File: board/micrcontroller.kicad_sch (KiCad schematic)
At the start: 20 parts, among them J2 USB_C_Receptacle_USB2.0_14P, SW1 SW_Push, U2 ESP32-S3-WROOM-1, U3 TXB0106PW

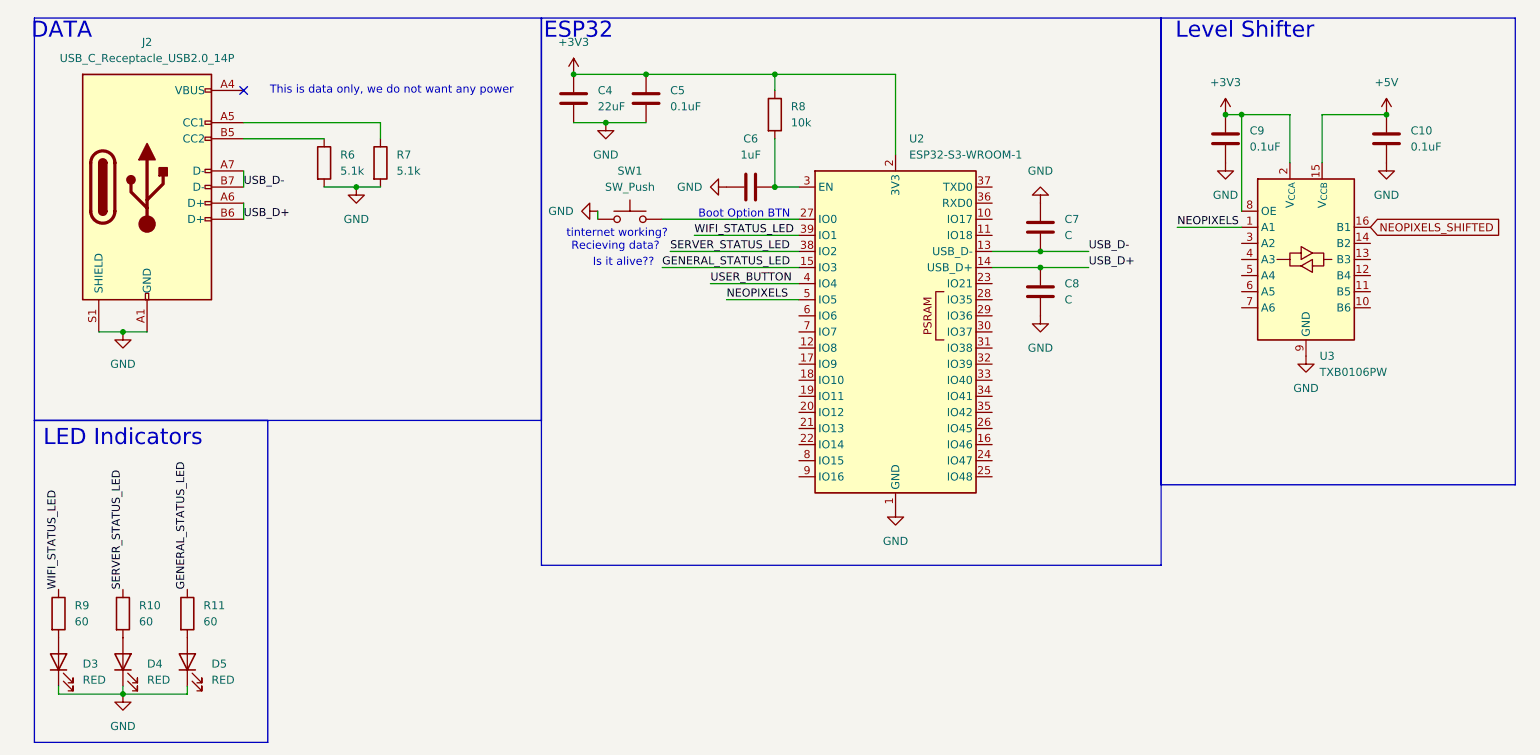
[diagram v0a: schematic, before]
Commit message: Display Schematic
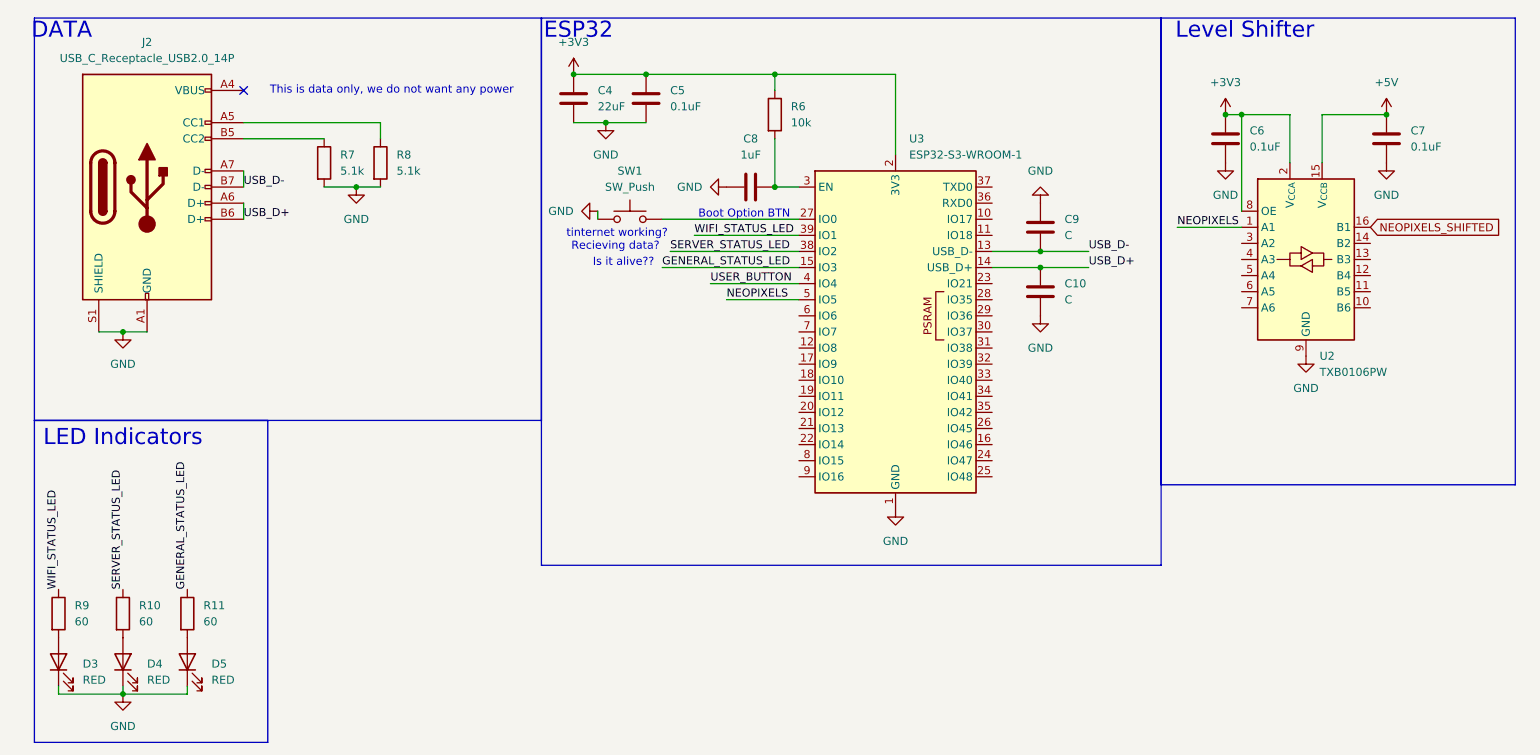
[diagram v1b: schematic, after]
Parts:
- renumbered C8 to C10, C9 to C6, C10 to C7, C6 to C8, C7 to C9, R8 to R6, R6 to R7, R7 to R8, U3 to U2, U2 to U3
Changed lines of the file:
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@@
 		(dnp no)
 		(fields_autoplaced yes)
-		(property "Reference" "#PWR015"
+		(property "Reference" "#PWR012"
 			(at 97.79 25.4 0)
 			(effects
@@
 			(project ""
 				(path "/380d0889-29f1-4d98-b1bb-ce6ede3c8d67/be360d18-9fa9-4ffe-af54-9dec7a1cbe21"
-					(reference "#PWR015")
+					(reference "#PWR012")
 					(unit 1)
 				)
@@
 		(dnp no)
 		(fields_autoplaced yes)
-		(property "Reference" "#PWR024"
+		(property "Reference" "#PWR017"
 			(at 226.06 41.91 0)
 			(effects
@@
 			(project ""
 				(path "/380d0889-29f1-4d98-b1bb-ce6ede3c8d67/be360d18-9fa9-4ffe-af54-9dec7a1cbe21"
-					(reference "#PWR024")
+					(reference "#PWR017")
 					(unit 1)
 				)
@@
 		(dnp no)
 		(fields_autoplaced yes)
-		(property "Reference" "#PWR014"
+		(property "Reference" "#PWR025"
 			(at 148.59 96.52 0)
 			(effects
@@
 			(project ""
 				(path "/380d0889-29f1-4d98-b1bb-ce6ede3c8d67/be360d18-9fa9-4ffe-af54-9dec7a1cbe21"
-					(reference "#PWR014")
+					(reference "#PWR025")
 					(unit 1)
 				)
@@
 		(dnp no)
 		(fields_autoplaced yes)
-		(property "Reference" "U2"
+		(property "Reference" "U3"
 			(at 150.7333 31.75 0)
 			(effects
@@
 			(project ""
 				(path "/380d0889-29f1-4d98-b1bb-ce6ede3c8d67/be360d18-9fa9-4ffe-af54-9dec7a1cbe21"
-					(reference "U2")
+					(reference "U3")
 					(unit 1)
 				)
@@
 		(dnp no)
 		(fields_autoplaced yes)
-		(property "Reference" "#PWR016"
+		(property "Reference" "#PWR015"
 			(at 102.87 35.56 0)
 			(effects
@@
 			(project ""
 				(path "/380d0889-29f1-4d98-b1bb-ce6ede3c8d67/be360d18-9fa9-4ffe-af54-9dec7a1cbe21"
-					(reference "#PWR016")
+					(reference "#PWR015")
 					(unit 1)
 				)
@@
 		(dnp no)
 		(fields_autoplaced yes)
-		(property "Reference" "#PWR023"
+		(property "Reference" "#PWR014"
 			(at 226.06 31.75 0)
 			(effects
@@
 			(project ""
 				(path "/380d0889-29f1-4d98-b1bb-ce6ede3c8d67/be360d18-9fa9-4ffe-af54-9dec7a1cbe21"
-					(reference "#PWR023")
+					(reference "#PWR014")
 					(unit 1)
 				)
@@
 		(dnp no)
 		(fields_autoplaced yes)
-		(property "Reference" "C10"
+		(property "Reference" "C7"
 			(at 229.87 30.4799 0)
 			(effects
@@
 			(project "board"
 				(path "/380d0889-29f1-4d98-b1bb-ce6ede3c8d67/be360d18-9fa9-4ffe-af54-9dec7a1cbe21"
-					(reference "C10")
+					(reference "C7")
 					(unit 1)
 				)
@@
 		(dnp no)
 		(fields_autoplaced yes)
-		(property "Reference" "U3"
+		(property "Reference" "U2"
 			(at 215.5033 66.04 0)
 			(effects
@@
 			(project ""
 				(path "/380d0889-29f1-4d98-b1bb-ce6ede3c8d67/be360d18-9fa9-4ffe-af54-9dec7a1cbe21"
-					(reference "U3")
+					(reference "U2")
 					(unit 1)
 				)
@@
 		(dnp no)
 		(fields_autoplaced yes)
-		(property "Reference" "#PWR017"
+		(property "Reference" "#PWR019"
 			(at 115.57 39.37 0)
 			(effects
@@
 			(project "board"
 				(path "/380d0889-29f1-4d98-b1bb-ce6ede3c8d67/be360d18-9fa9-4ffe-af54-9dec7a1cbe21"
-					(reference "#PWR017")
+					(reference "#PWR019")
 					(unit 1)
 				)
@@
 		(dnp no)
 		(fields_autoplaced yes)
-		(property "Reference" "R6"
+		(property "Reference" "R7"
 			(at 60.96 34.2899 0)
 			(effects
@@
 			(project ""
 				(path "/380d0889-29f1-4d98-b1bb-ce6ede3c8d67/be360d18-9fa9-4ffe-af54-9dec7a1cbe21"
-					(reference "R6")
+					(reference "R7")
 					(unit 1)
 				)
@@
 		(dnp no)
 		(fields_autoplaced yes)
-		(property "Reference" "#PWR021"
+		(property "Reference" "#PWR026"
 			(at 26.67 125.73 0)
 			(effects
@@
 			(project ""
 				(path "/380d0889-29f1-4d98-b1bb-ce6ede3c8d67/be360d18-9fa9-4ffe-af54-9dec7a1cbe21"
-					(reference "#PWR021")
+					(reference "#PWR026")
 					(unit 1)
 				)
@@
 		(dnp no)
 		(fields_autoplaced yes)
-		(property "Reference" "#PWR012"
+		(property "Reference" "#PWR023"
 			(at 26.67 68.58 0)
 			(effects
@@
 			(project ""
 				(path "/380d0889-29f1-4d98-b1bb-ce6ede3c8d67/be360d18-9fa9-4ffe-af54-9dec7a1cbe21"
-					(reference "#PWR012")
+					(reference "#PWR023")
 					(unit 1)
 				)
@@
 		(dnp no)
 		(fields_autoplaced yes)
-		(property "Reference" "R8"
+		(property "Reference" "R6"
 			(at 132.08 26.6699 0)
 			(effects
@@
 			(project ""
 				(path "/380d0889-29f1-4d98-b1bb-ce6ede3c8d67/be360d18-9fa9-4ffe-af54-9dec7a1cbe21"
-					(reference "R8")
+					(reference "R6")
 					(unit 1)
 				)
@@
 		(dnp no)
 		(fields_autoplaced yes)
-		(property "Reference" "#PWR018"
+		(property "Reference" "#PWR021"
 			(at 95.25 43.18 0)
 			(effects
@@
 			(project ""
 				(path "/380d0889-29f1-4d98-b1bb-ce6ede3c8d67/be360d18-9fa9-4ffe-af54-9dec7a1cbe21"
-					(reference "#PWR018")
+					(reference "#PWR021")
 					(unit 1)
 				)
@@
 		(dnp no)
 		(fields_autoplaced yes)
-		(property "Reference" "#PWR019"
+		(property "Reference" "#PWR022"
 			(at 171.45 66.04 0)
 			(effects
@@
 			(project "board"
 				(path "/380d0889-29f1-4d98-b1bb-ce6ede3c8d67/be360d18-9fa9-4ffe-af54-9dec7a1cbe21"
-					(reference "#PWR019")
+					(reference "#PWR022")
 					(unit 1)
 				)
@@
 		(dnp no)
 		(fields_autoplaced yes)
-		(property "Reference" "C8"
+		(property "Reference" "C10"
 			(at 175.26 54.6099 0)
 			(effects
@@
 			(project "board"
 				(path "/380d0889-29f1-4d98-b1bb-ce6ede3c8d67/be360d18-9fa9-4ffe-af54-9dec7a1cbe21"
-					(reference "C8")
+					(reference "C10")
 					(unit 1)
 				)
@@
 		(dnp no)
 		(fields_autoplaced yes)
-		(property "Reference" "#PWR026"
+		(property "Reference" "#PWR024"
 			(at 213.36 72.39 0)
 			(effects
@@
 			(project "board"
 				(path "/380d0889-29f1-4d98-b1bb-ce6ede3c8d67/be360d18-9fa9-4ffe-af54-9dec7a1cbe21"
-					(reference "#PWR026")
+					(reference "#PWR024")
 					(unit 1)
 				)
@@
 		(dnp no)
 		(fields_autoplaced yes)
-		(property "Reference" "R7"
+		(property "Reference" "R8"
 			(at 69.85 34.2899 0)
 			(effects
@@
 			(project "board"
 				(path "/380d0889-29f1-4d98-b1bb-ce6ede3c8d67/be360d18-9fa9-4ffe-af54-9dec7a1cbe21"
-					(reference "R7")
+					(reference "R8")
 					(unit 1)
 				)
@@
 		(dnp no)
 		(fields_autoplaced yes)
-		(property "Reference" "#PWR025"
+		(property "Reference" "#PWR016"
 			(at 200.66 41.91 0)
 			(effects
@@
 			(project "board"
 				(path "/380d0889-29f1-4d98-b1bb-ce6ede3c8d67/be360d18-9fa9-4ffe-af54-9dec7a1cbe21"
-					(reference "#PWR025")
+					(reference "#PWR016")
 					(unit 1)
 				)
@@
 		(dnp no)
 		(fields_autoplaced yes)
-		(property "Reference" "C7"
+		(property "Reference" "C9"
 			(at 175.26 44.4499 0)
 			(effects
@@
 			(project ""
 				(path "/380d0889-29f1-4d98-b1bb-ce6ede3c8d67/be360d18-9fa9-4ffe-af54-9dec7a1cbe21"
-					(reference "C7")
+					(reference "C9")
 					(unit 1)
 				)
@@
 		(dnp no)
 		(fields_autoplaced yes)
-		(property "Reference" "#PWR013"
+		(property "Reference" "#PWR018"
 			(at 63.5 45.72 0)
 			(effects
@@
 			(project ""
 				(path "/380d0889-29f1-4d98-b1bb-ce6ede3c8d67/be360d18-9fa9-4ffe-af54-9dec7a1cbe21"
-					(reference "#PWR013")
+					(reference "#PWR018")
 					(unit 1)
 				)
@@
 		(dnp no)
 		(fields_autoplaced yes)
-		(property "Reference" "#PWR022"
+		(property "Reference" "#PWR013"
 			(at 200.66 31.75 0)
 			(effects
@@
 			(project ""
 				(path "/380d0889-29f1-4d98-b1bb-ce6ede3c8d67/be360d18-9fa9-4ffe-af54-9dec7a1cbe21"
-					(reference "#PWR022")
+					(reference "#PWR013")
 					(unit 1)
 				)
@@
 		(dnp no)
 		(fields_autoplaced yes)
-		(property "Reference" "C9"
+		(property "Reference" "C6"
 			(at 204.47 30.4799 0)
 			(effects
@@
 			(project ""
 				(path "/380d0889-29f1-4d98-b1bb-ce6ede3c8d67/be360d18-9fa9-4ffe-af54-9dec7a1cbe21"
-					(reference "C9")
+					(reference "C6")
 					(unit 1)
 				)
@@
 		(dnp no)
 		(fields_autoplaced yes)
-		(property "Reference" "C6"
+		(property "Reference" "C8"
 			(at 125.73 31.75 90)
 			(effects
@@
 			(project "board"
 				(path "/380d0889-29f1-4d98-b1bb-ce6ede3c8d67/be360d18-9fa9-4ffe-af54-9dec7a1cbe21"
-					(reference "C6")
-					(unit 1)
-				)
+					(reference "C8")
+					(unit 1)
+				)

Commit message: Lots of silly train things
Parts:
- added SW2: SW_Push, LCSC:SW-SMD_4P-L4.2-W3.3-P2.15-LS5.1, symbol Switch:SW_Push
- C10, C4, C5, C6, C7, C8, C9: footprint (none) -> Capacitor_SMD:C_0805_2012Metric
- D3, D4, D5: footprint (none) -> LED_SMD:LED_0805_2012Metric
- J2: footprint (none) -> Connector_USB:USB_C_Receptacle_G-Switch_GT-USB-7010ASV
- R10, R11, R6, R7, R8, R9: footprint (none) -> Resistor_SMD:R_0805_2012Metric
- SW1: footprint (none) -> LCSC:SW-SMD_4P-L4.2-W3.3-P2.15-LS5.1
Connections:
- net GND: now also SW2.1
- net USER_BUTTON: now also SW2.2
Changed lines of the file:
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@@
+		)
+	)
+	(label "USER_BUTTON"
+		(at 81.28 90.17 90)
+		(effects
+			(font
+				(size 1.27 1.27)
+			)
+			(justify left bottom)
 		)
 	)
@@
 			)
 		)
-		(property "Footprint" ""
+		(property "Footprint" "LED_SMD:LED_0805_2012Metric"
 			(at 36.83 114.3 0)
 			(effects
@@
 	(symbol
 		(lib_id "power:GND")
+		(at 81.28 100.33 0)
+		(unit 1)
+		(exclude_from_sim no)
+		(in_bom yes)
+		(on_board yes)
+		(dnp no)
+		(fields_autoplaced yes)
+		(property "Reference" "#PWR072"
+			(at 81.28 106.68 0)
+			(effects
+				(font
+					(size 1.27 1.27)
+				)
+				(hide yes)
+			)
+		)
+		(property "Value" "GND"
+			(at 81.28 105.41 0)
+			(effects
+				(font
+					(size 1.27 1.27)
+				)
+			)
+		)
+		(property "Footprint" ""
+			(at 81.28 100.33 0)
+			(effects
+				(font
+					(size 1.27 1.27)
+				)
+				(hide yes)
+			)
+		)
+		(property "Datasheet" ""
+			(at 81.28 100.33 0)
+			(effects
+				(font
+					(size 1.27 1.27)
+				)
+				(hide yes)
+			)
+		)
+		(property "Description" "Power symbol creates a global label with name \"GND\" , ground"
+			(at 81.28 100.33 0)
+			(effects
+				(font
+					(size 1.27 1.27)
+				)
+				(hide yes)
+			)
+		)
+		(pin "1"
+		)
+		(instances
+			(project "board"
+				(path "/380d0889-29f1-4d98-b1bb-ce6ede3c8d67/be360d18-9fa9-4ffe-af54-9dec7a1cbe21"
+					(reference "#PWR072")
+					(unit 1)
+				)
+			)
+		)
+	)
+	(symbol
+		(lib_id "power:GND")
 		(at 102.87 29.21 0)
 		(unit 1)
@@
 			)
 		)
-		(property "Footprint" ""
+		(property "Footprint" "LCSC:SW-SMD_4P-L4.2-W3.3-P2.15-LS5.1"
 			(at 106.68 39.37 0)
 			(effects
@@
 			)
 		)
-		(property "Footprint" ""
+		(property "Footprint" "Capacitor_SMD:C_0805_2012Metric"
 			(at 227.0252 35.56 0)
 			(effects
@@
 			)
 		)
-		(property "Footprint" ""
+		(property "Footprint" "LED_SMD:LED_0805_2012Metric"
 			(at 16.51 114.3 0)
 			(effects
@@
 			)
 		)
-		(property "Footprint" ""
+		(property "Footprint" "Capacitor_SMD:C_0805_2012Metric"
 			(at 110.1852 29.21 0)
 			(effects
@@
 			)
 		)
-		(property "Footprint" ""
+		(property "Footprint" "Resistor_SMD:R_0805_2012Metric"
 			(at 56.642 35.56 90)
 			(effects
@@
 			)
 		)
-		(property "Footprint" ""
+		(property "Footprint" "Connector_USB:USB_C_Receptacle_G-Switch_GT-USB-7010ASV"
 			(at 34.29 39.37 0)
 			(effects
@@
 			)
 		)
-		(property "Footprint" ""
+		(property "Footprint" "Resistor_SMD:R_0805_2012Metric"
 			(at 127.762 27.94 90)
 			(effects
@@
 			)
 		)
-		(property "Footprint" ""
+		(property "Footprint" "Capacitor_SMD:C_0805_2012Metric"
 			(at 172.4152 59.69 0)
 			(effects
@@
 			)
 		)
-		(property "Footprint" ""
+		(property "Footprint" "Resistor_SMD:R_0805_2012Metric"
 			(at 14.732 106.68 90)
 			(effects
@@
 			)
 		)
-		(property "Footprint" ""
+		(property "Footprint" "Capacitor_SMD:C_0805_2012Metric"
 			(at 98.7552 29.21 0)
 			(effects
@@
 			)
 		)
-		(property "Footprint" ""
+		(property "Footprint" "Resistor_SMD:R_0805_2012Metric"
 			(at 24.892 106.68 90)
 			(effects
@@
 			)
 		)
-		(property "Footprint" ""
+		(property "Footprint" "Resistor_SMD:R_0805_2012Metric"
 			(at 65.532 35.56 90)
 			(effects
@@
 			)
 		)
-		(property "Footprint" ""
+		(property "Footprint" "LED_SMD:LED_0805_2012Metric"
 			(at 26.67 114.3 0)
 			(effects
@@
 			)
 		)
-		(property "Footprint" ""
+		(property "Footprint" "Capacitor_SMD:C_0805_2012Metric"
 			(at 172.4152 49.53 0)
 			(effects
@@
 	)
 	(symbol
+		(lib_id "Switch:SW_Push")
+		(at 81.28 95.25 90)
+		(unit 1)
+		(exclude_from_sim no)
+		(in_bom yes)
+		(on_board yes)
+		(dnp no)
+		(fields_autoplaced yes)
+		(property "Reference" "SW2"
+			(at 82.55 93.9799 90)
+			(effects
+				(font
+					(size 1.27 1.27)
+				)
+				(justify right)
+			)
+		)
+		(property "Value" "SW_Push"
+			(at 82.55 96.5199 90)
+			(effects
+				(font
+					(size 1.27 1.27)
+				)
+				(justify right)
+			)
+		)
+		(property "Footprint" "LCSC:SW-SMD_4P-L4.2-W3.3-P2.15-LS5.1"
+			(at 76.2 95.25 0)
+			(effects
+				(font
+					(size 1.27 1.27)
+				)
+				(hide yes)
+			)
+		)
+		(property "Datasheet" "~"
+			(at 76.2 95.25 0)
+			(effects
+				(font
+					(size 1.27 1.27)
+				)
+				(hide yes)
+			)
+		)
+		(property "Description" "Push button switch, generic, two pins"
+			(at 81.28 95.25 0)
+			(effects
+				(font
+					(size 1.27 1.27)
+				)
+				(hide yes)
+			)
+		)
+		(pin "2"
+		)
+		(pin "1"
+		)
+		(instances
+			(project "board"
+				(path "/380d0889-29f1-4d98-b1bb-ce6ede3c8d67/be360d18-9fa9-4ffe-af54-9dec7a1cbe21"
+					(reference "SW2")
+					(unit 1)
+				)
+			)
+		)
+	)
+	(symbol
 		(lib_id "power:+3V3")
 		(at 200.66 27.94 0)
@@
 			)
 		)
-		(property "Footprint" ""
+		(property "Footprint" "Capacitor_SMD:C_0805_2012Metric"
 			(at 201.6252 35.56 0)
 			(effects
@@
 			)
 		)
-		(property "Footprint" ""
+		(property "Footprint" "Capacitor_SMD:C_0805_2012Metric"
 			(at 121.92 40.3352 0)
 			(effects
@@
 			)
 		)
-		(property "Footprint" ""
+		(property "Footprint" "Resistor_SMD:R_0805_2012Metric"
 			(at 35.052 106.68 90)
 			(effects

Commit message: Micrcontroller, but wired up
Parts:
- added C13: 0.1uF, Capacitor_SMD:C_0805_2012Metric, symbol Device:C
- added SW3: SW_Push, LCSC:SW-SMD_4P-L4.2-W3.3-P2.15-LS5.1, symbol Switch:SW_Push
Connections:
- net GENERAL_STATUS_LED: now also U3.5 (IO5); no longer U3.15 (IO3)
- net GND: now also C13.1, SW3.1
- net NEOPIXELS: now also U3.15 (IO3); no longer U3.5 (IO5)
- net SERVER_STATUS_LED: now also U3.6 (IO6); no longer U3.38 (IO2)
- net WIFI_STATUS_LED: now also U3.7 (IO7); no longer U3.39 (IO1)
- net EN: now reaches C8.1, R6.2, U3.3 (EN)
- net EN: now also C13.2, SW3.2
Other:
- note added: "RESET"
